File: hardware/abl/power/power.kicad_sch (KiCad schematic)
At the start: 30 parts, among them J1 Screw_Terminal_01x03, J2 Screw_Terminal_01x03, J3 Barrel_Jack, J4 Screw_Terminal_01x03, J6 009159008603906, U1 IRM-45-5, U2 IRM-30-5, U3 INA219AxD, U4 TMP1075D, U5 TWGMC AMS1117-3.3

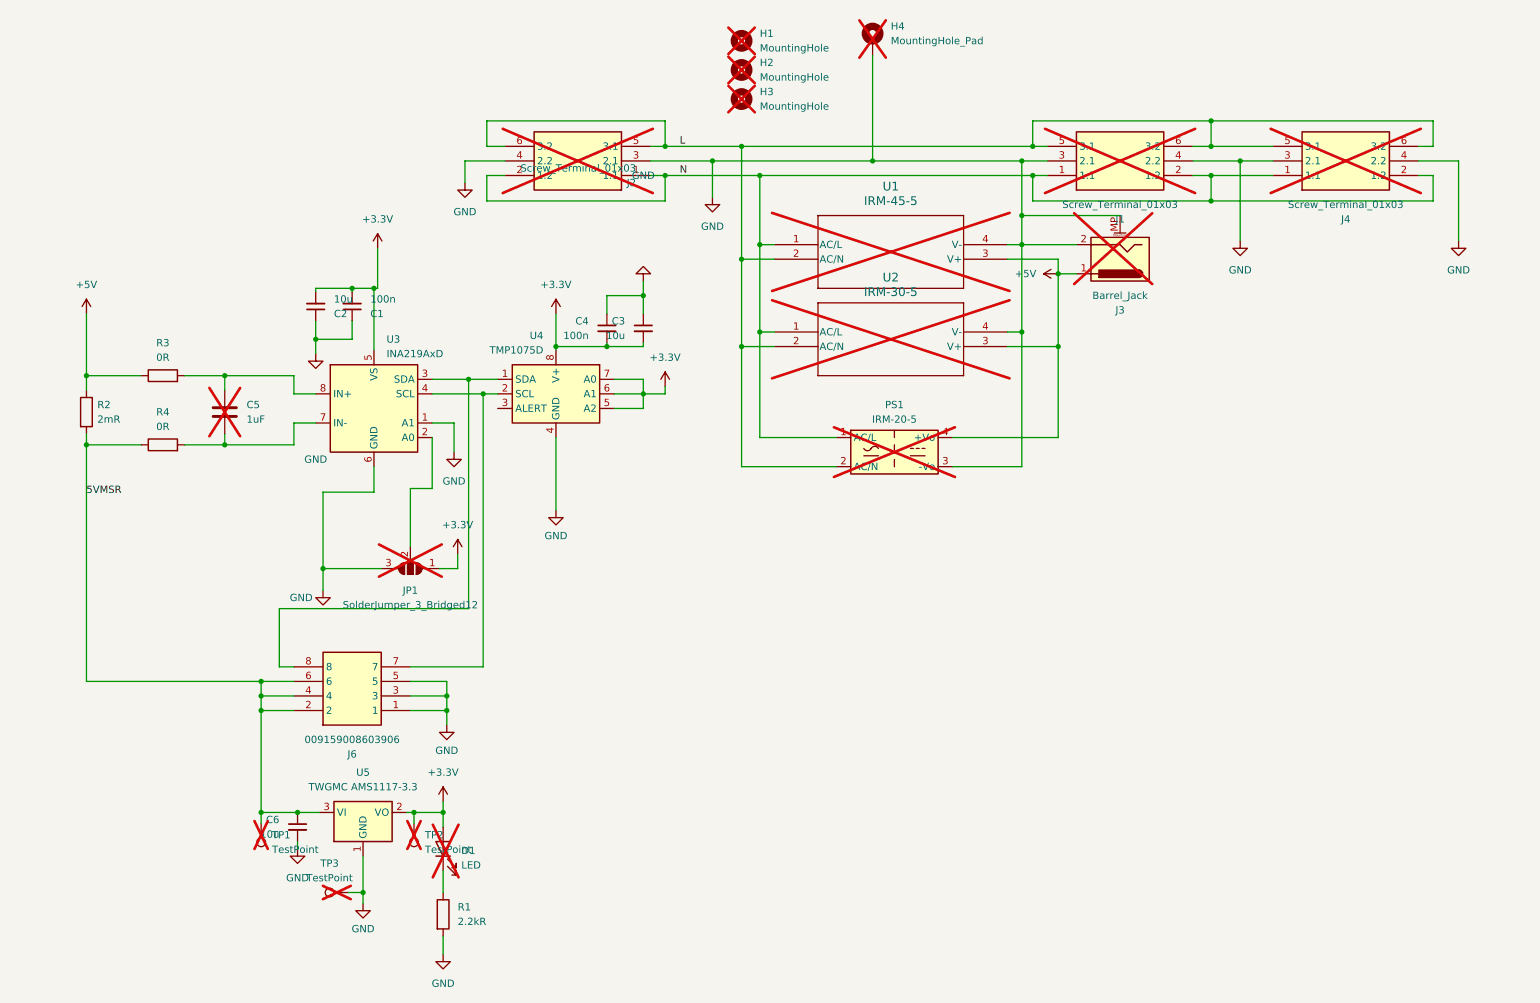
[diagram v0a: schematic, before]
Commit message: Clean up schematics and minor fixes in PCB layouts.
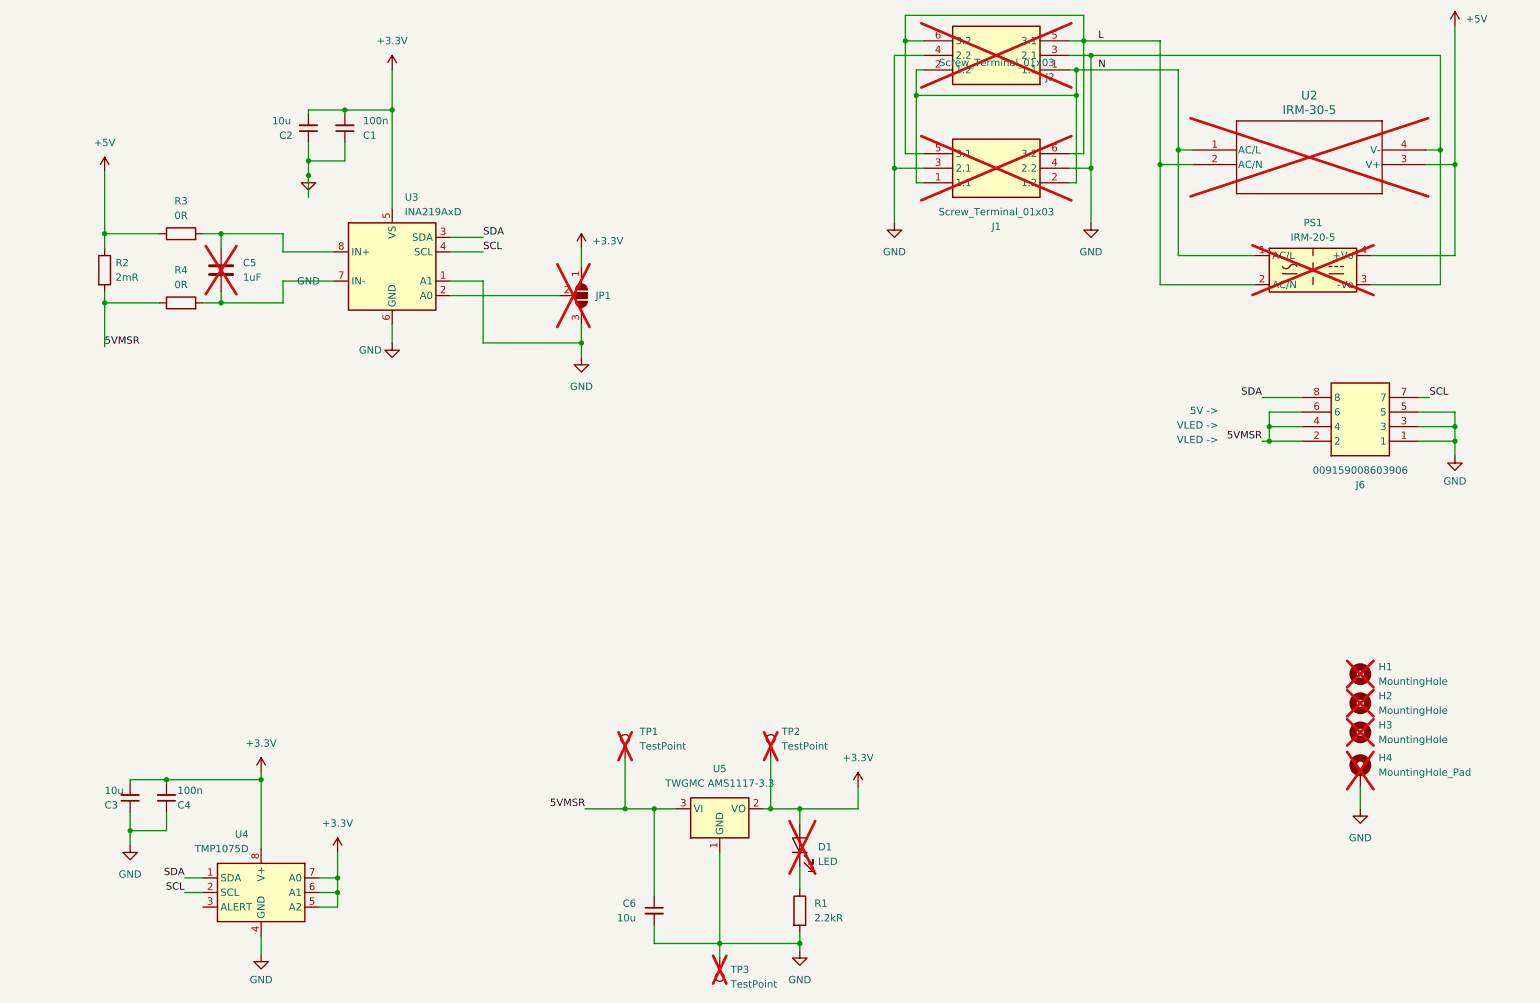
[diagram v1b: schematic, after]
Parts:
- removed J3: Barrel_Jack, Connector_BarrelJack:BarrelJack_CUI_PJ-063AH_Horizontal_CircularHoles, symbol Connector:Barrel_Jack_MountingPin
- removed J4: Screw_Terminal_01x03, WAGO-2604-1103:26041103, symbol WAGO-2604-1103:2604-1103
- removed U1: IRM-45-5, IRM-45:IRM-45_MWU, symbol Meanwell IRM-45:IRM-45-5
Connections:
- net SDA: now reaches J6.8, U3.3 (SDA), U4.1 (SDA)
- net SCL: now reaches J6.7, U3.4 (SCL), U4.2 (SCL)
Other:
- note added: "5V ->"
- note added: "VLED ->"
- moved on the sheet: C1, C2, C3, C4, C5, C6, D1, H1, H2, H3, H4, J1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

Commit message: Separate GND from earth protective.
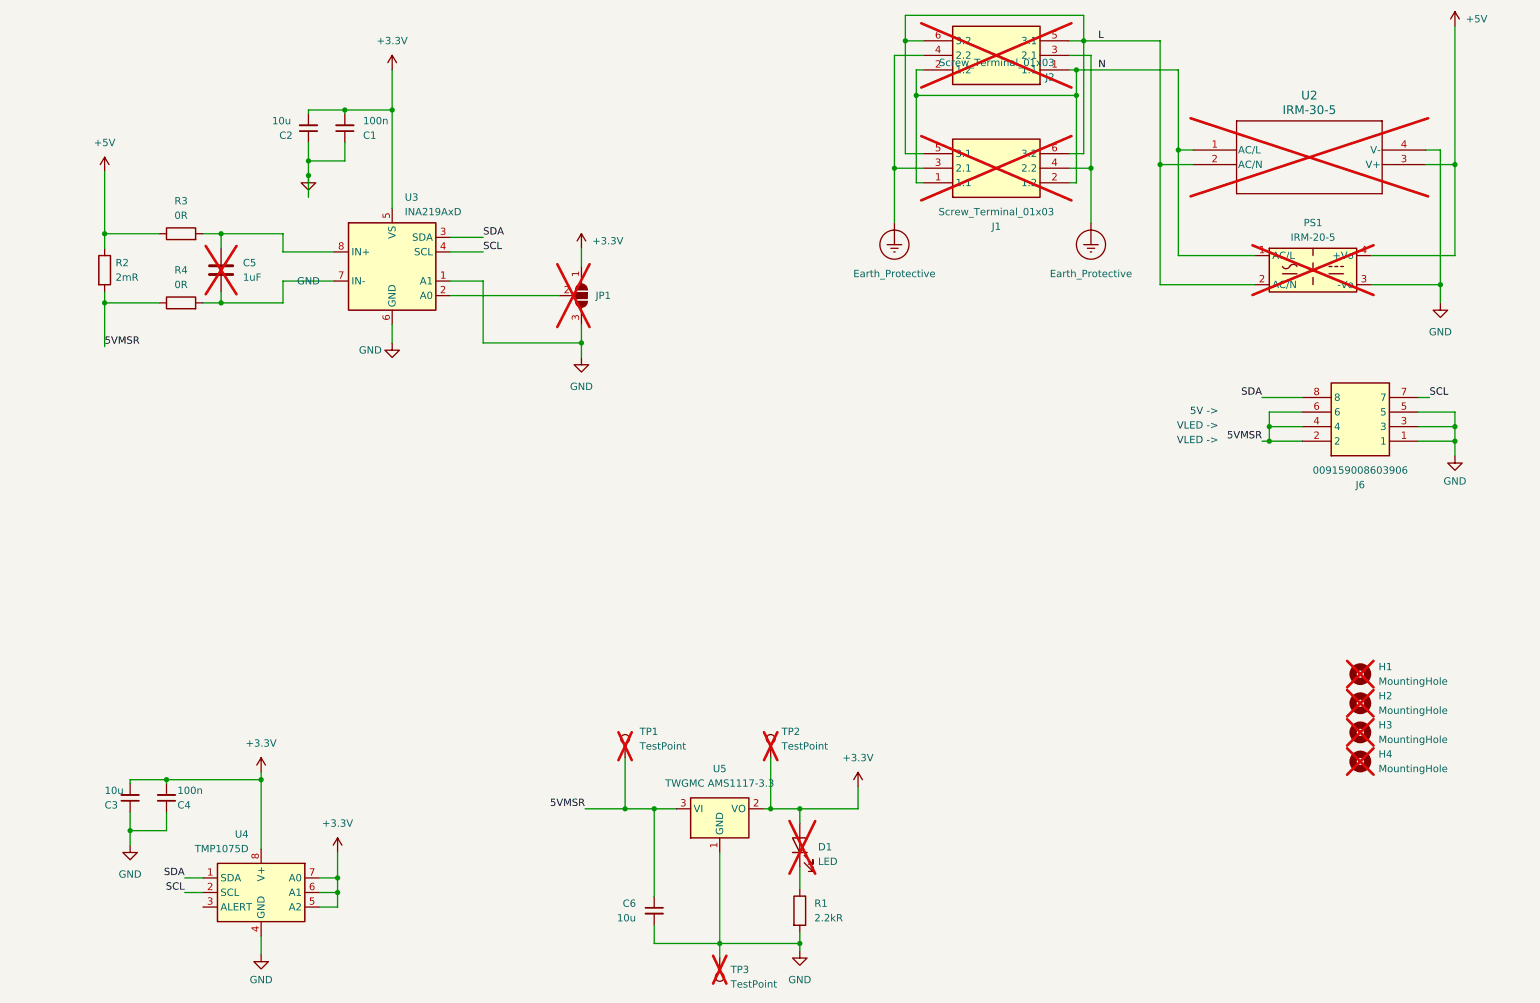
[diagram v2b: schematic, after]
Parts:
- removed H4: MountingHole_Pad, MountingHole:MountingHole_3.2mm_M3_DIN965_Pad, symbol Mechanical:MountingHole_Pad
- added H4: MountingHole, MountingHole:MountingHole_3.2mm_M3_DIN965, symbol Mechanical:MountingHole
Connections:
- net GND: no longer J1.3 (2.1), J1.4 (2.2), J2.3 (2.1), J2.4 (2.2)
- new net Earth_Protective: J1.3 (2.1), J1.4 (2.2), J2.3 (2.1), J2.4 (2.2)

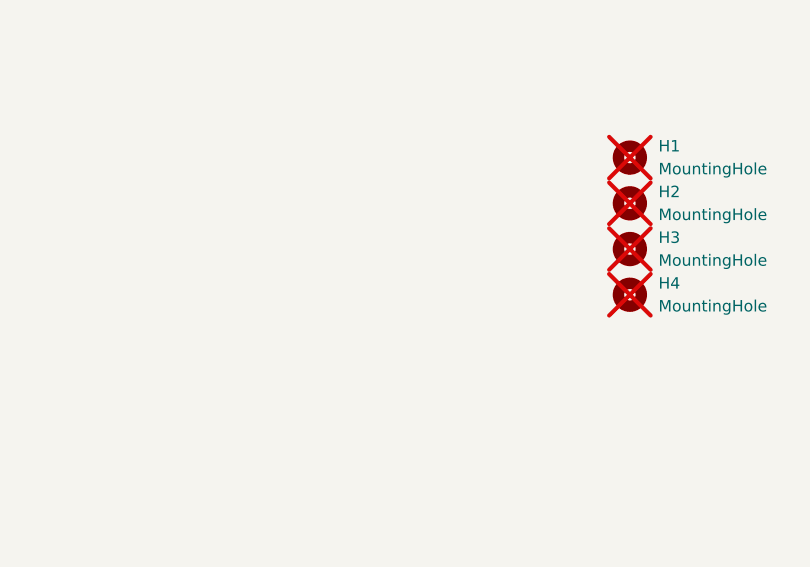
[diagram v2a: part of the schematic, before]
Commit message: Enlarged PCB at the top to add protective earth connector, optimized traces and I2C return paths.
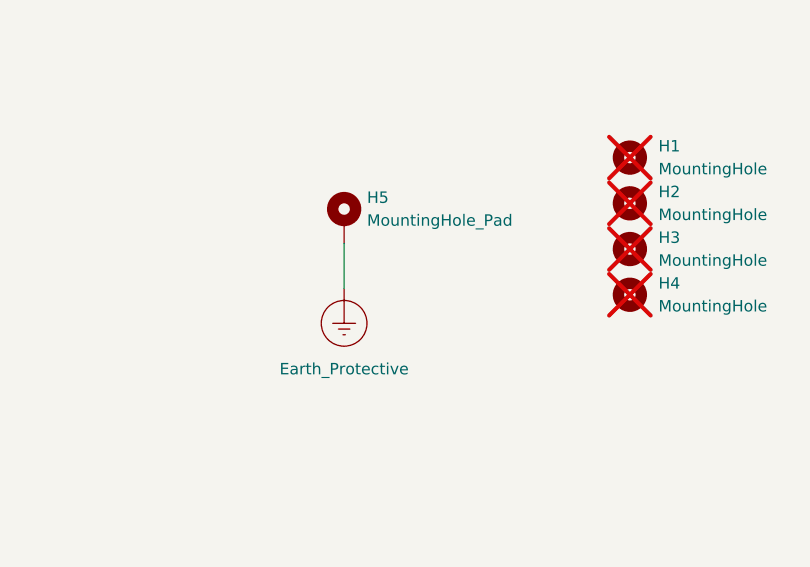
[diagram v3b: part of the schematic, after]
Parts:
- added H5: MountingHole_Pad, MountingHole:MountingHole_5.3mm_M5_DIN965_Pad_TopOnly, symbol Mechanical:MountingHole_Pad
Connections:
- net Earth_Protective: now also H5.1
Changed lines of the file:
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@@
+	(wire
+		(pts
+			(xy 218.44 144.78) (xy 218.44 149.86)
+		)
+		(stroke
+			(width 0)
+			(type default)
+		)
+	)
 	(wire
 		(pts
@@
 	)
 	(symbol
+		(lib_id "power:Earth_Protective")
+		(at 218.44 149.86 0)
+		(unit 1)
+		(exclude_from_sim no)
+		(in_bom yes)
+		(on_board yes)
+		(dnp no)
+		(fields_autoplaced yes)
+		(property "Reference" "#PWR06"
+			(at 218.44 160.02 0)
+			(effects
+				(font
+					(size 1.27 1.27)
+				)
+				(hide yes)
+			)
+		)
+		(property "Value" "Earth_Protective"
+			(at 218.44 158.75 0)
+			(effects
+				(font
+					(size 1.27 1.27)
+				)
+			)
+		)
+		(property "Footprint" ""
+			(at 218.44 152.4 0)
+			(effects
+				(font
+					(size 1.27 1.27)
+				)
+				(hide yes)
+			)
+		)
+		(property "Datasheet" "~"
+			(at 218.44 152.4 0)
+			(effects
+				(font
+					(size 1.27 1.27)
+				)
+				(hide yes)
+			)
+		)
+		(property "Description" "Power symbol creates a global label with name \"Earth_Protective\""
+			(at 218.44 149.86 0)
+			(effects
+				(font
+					(size 1.27 1.27)
+				)
+				(hide yes)
+			)
+		)
+		(pin "1"
+		)
+		(instances
+			(project "power"
+				(path "/158daa50-c9fc-49fb-a041-1822899d5deb"
+					(reference "#PWR06")
+					(unit 1)
+				)
+			)
+		)
+	)
+	(symbol
 		(lib_id "power:+3.3V")
 		(at 81.28 29.845 0)
@@
 					(unit 1)
 				)
+			)
+		)
+	)
+	(symbol
+		(lib_id "Mechanical:MountingHole_Pad")
+		(at 218.44 142.24 0)
+		(unit 1)
+		(exclude_from_sim yes)
+		(in_bom no)
+		(on_board yes)
+		(dnp no)
+		(fields_autoplaced yes)
+		(property "Reference" "H5"
+			(at 220.98 139.6999 0)
+			(effects
+				(font
+					(size 1.27 1.27)
+				)
+				(justify left)
+			)
+		)
+		(property "Value" "MountingHole_Pad"
+			(at 220.98 142.2399 0)
+			(effects
+				(font
+					(size 1.27 1.27)
+				)
+				(justify left)
+			)
+		)
+		(property "Footprint" "MountingHole:MountingHole_5.3mm_M5_DIN965_Pad_TopOnly"
+			(at 218.44 142.24 0)
+			(effects
+				(font
+					(size 1.27 1.27)
+				)
+				(hide yes)
+			)
+		)
+		(property "Datasheet" "~"
+			(at 218.44 142.24 0)
+			(effects
+				(font
+					(size 1.27 1.27)
+				)
+				(hide yes)
+			)
+		)
+		(property "Description" "Mounting Hole with connection"
+			(at 218.44 142.24 0)
+			(effects
+				(font
+					(size 1.27 1.27)
+				)
+				(hide yes)
+			)
+		)
+		(pin "1"
+		)
+		(instances
+			(project "power"
+				(path "/158daa50-c9fc-49fb-a041-1822899d5deb"
+					(reference "H5")
+					(unit 1)
+				)

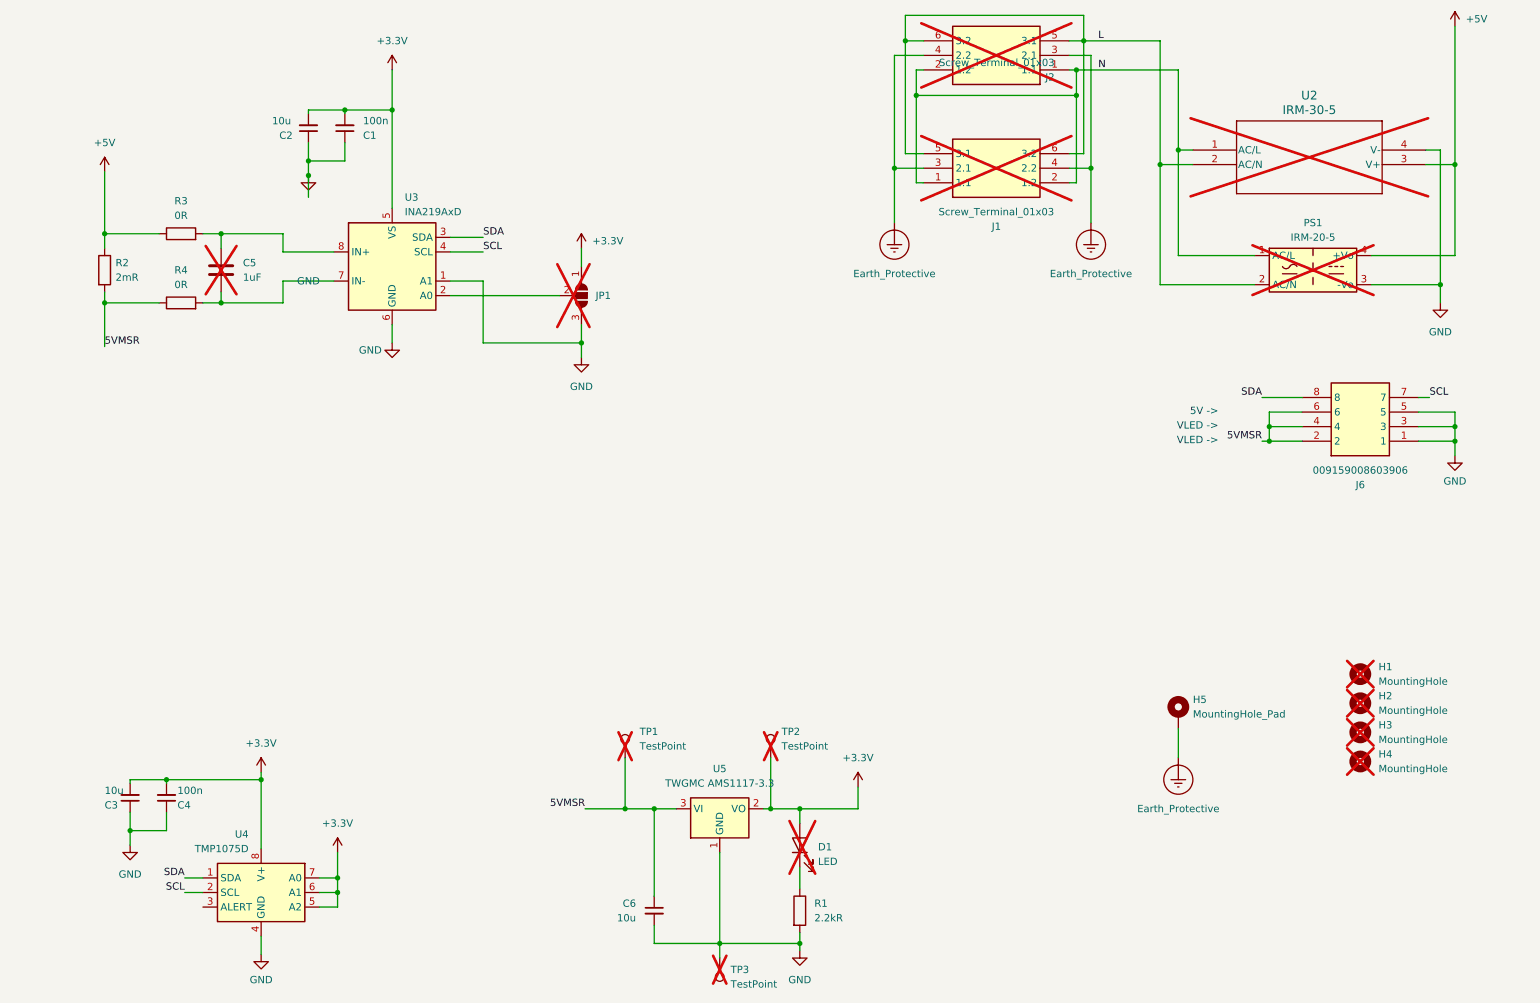
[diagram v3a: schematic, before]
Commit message: Revert board size, swap some mounting holes and protective earth, fix swapped N and L wires.
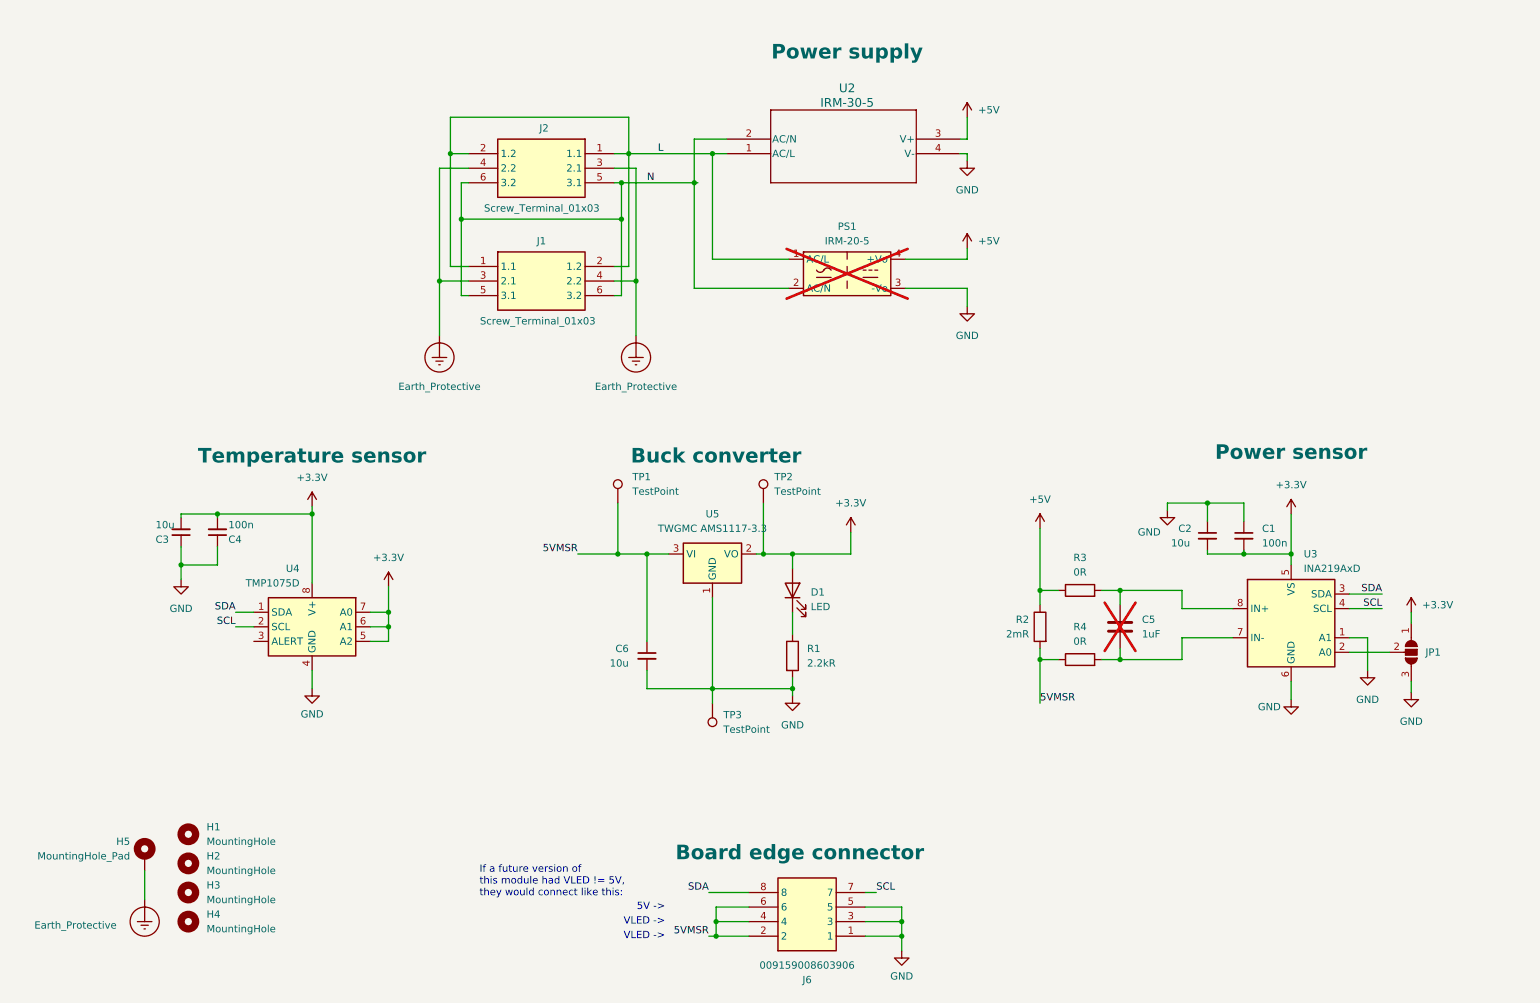
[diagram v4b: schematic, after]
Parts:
- D1, H1, H2, H3, H4, J1, J2, JP1, TP1, TP2, TP3: now fitted
- J6: Purpose (none) -> Board edge connector
- PS1: Purpose (none) -> Power supply
- U2: Purpose (none) -> Power supply; now fitted
- U3: Purpose (none) -> Power sensor
- U4: Purpose (none) -> Temperature sensor
- U5: Purpose (none) -> Buck converter
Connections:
- net L: now also J1.1 (1.1), J1.2 (1.2), J2.1 (1.1), J2.2 (1.2), PS1.1 (AC/L), U2.1 (AC/L); no longer J1.5 (3.1), J1.6 (3.2), J2.5 (3.1), J2.6 (3.2), PS1.2 (AC/N), U2.2 (AC/N)
- net N: now also J1.5 (3.1), J1.6 (3.2), J2.5 (3.1), J2.6 (3.2), PS1.2 (AC/N), U2.2 (AC/N); no longer J1.1 (1.1), J1.2 (1.2), J2.1 (1.1), J2.2 (1.2), PS1.1 (AC/L), U2.1 (AC/L)
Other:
- note added: "If a future version of this module had VLED != 5V, they would connect like this:"
- moved on the sheet: C1, C2, C3, C4, C5, C6, H5, J6, PS1, R1, R2, R3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

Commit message: Many small optimizations and cleanups.
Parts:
- added R5: 0R, Resistor_SMD:R_0805_2012Metric, symbol Device:R
- renumbered C6 to C1, C3 to C2, C4 to C3, C2 to C4, C1 to C5, C5 to C6, J6 to J3, U2 to PS2, U5 to U1, U4 to U2
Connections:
- net +5V: now also TP1.1
- net 5VMSR: no longer TP1.1
- net Earth_Protective: now also R5.1
- net GND: now also R5.2
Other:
- moved on the sheet: C1, C2, C3, D1, H5, R1, TP1, TP2, TP3, U1, U2
